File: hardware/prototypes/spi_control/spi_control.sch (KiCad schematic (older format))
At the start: 78 parts, among them J1 USB_B_Micro, J39 Versa_1, J40 Versa_2, U1 ST1L08SPU33R, U2 MCP2210-I_MQ, U3 ADAR7251, U4 BGT24_Module, Y1 12MHZ, Y2 40MHz

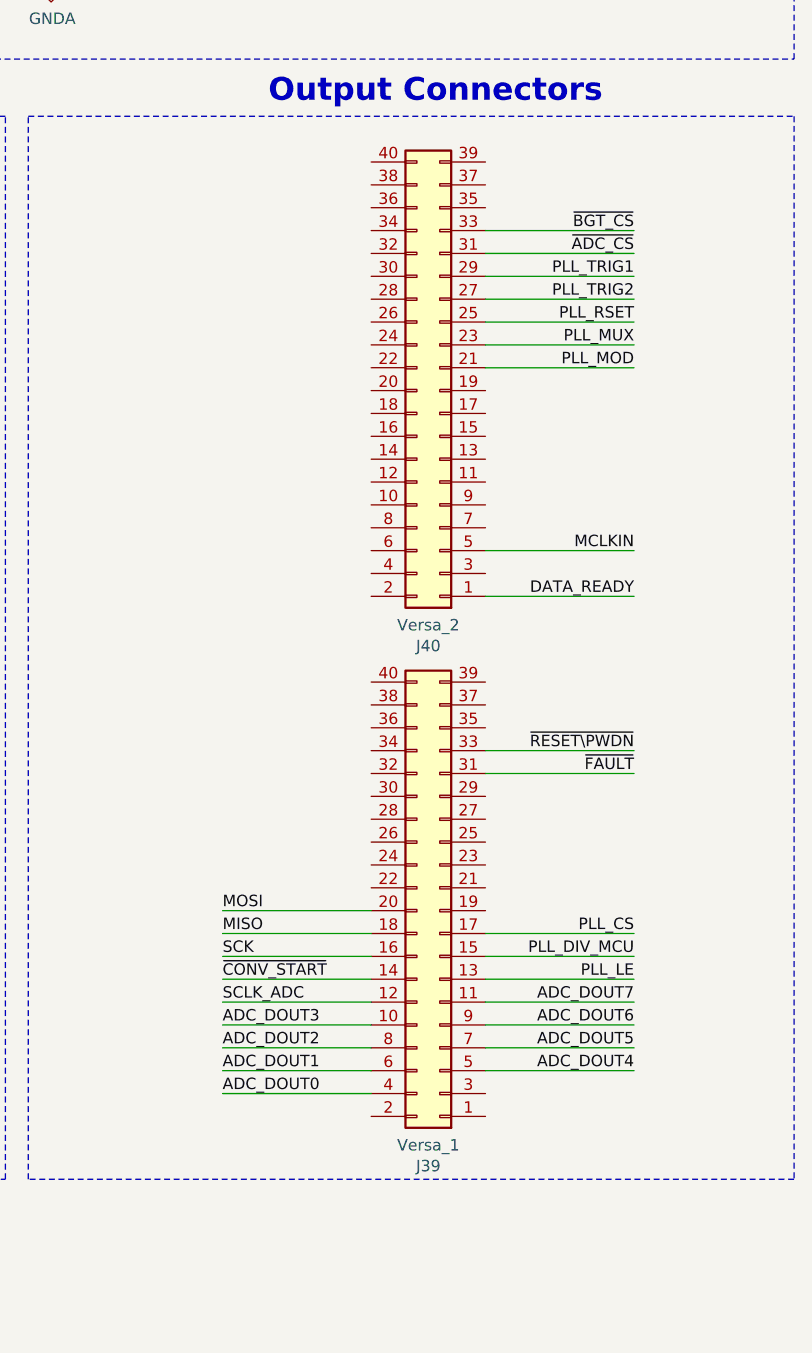
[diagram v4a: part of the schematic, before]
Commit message: Found mistake in header breakout, grounds were not connected. Fixed, layout and schematic.
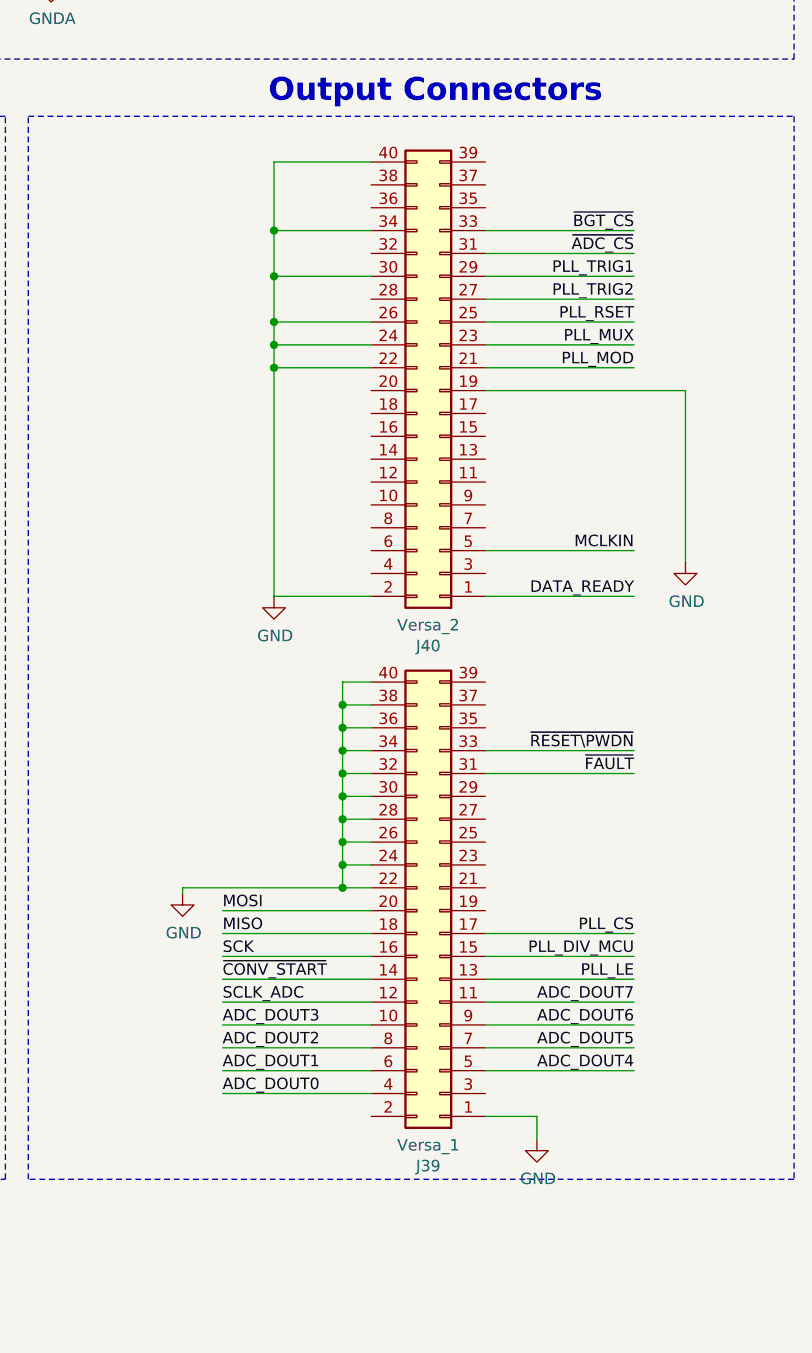
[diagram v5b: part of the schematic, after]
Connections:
- net GND: now also J39.1 (Pin_1), J39.22 (Pin_22), J39.24 (Pin_24), J39.26 (Pin_26), J39.28 (Pin_28), J39.30 (Pin_30), J39.32 (Pin_32), J39.34 (Pin_34), J39.36 (Pin_36), J39.38 (Pin_38), J39.40 (Pin_40), J40.19 (Pin_19), J40.2 (Pin_2), J40.22 (Pin_22), J40.24 (Pin_24), J40.26 (Pin_26), J40.30 (Pin_30), J40.34 (Pin_34), J40.40 (Pin_40)
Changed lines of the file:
@@
 EESchema Schematic File Version 4
 LIBS:spi_control-cache
-EELAYER 30 0
+EELAYER 29 0
 EELAYER END
 $Descr B 17000 11000
@@
 Text Notes 1550 3800 0    100  ~ 20
 RF Transceiver - BGT24 Module
+$Comp
+L power:GND #PWR?
+U 1 1 5DD3FA35
+P 13725 7950
+F 0 "#PWR?" H 13725 7700 50  0001 C CNN
+F 1 "GND" H 13730 7777 50  0000 C CNN
+F 2 "" H 13725 7950 50  0001 C CNN
+F 3 "" H 13725 7950 50  0001 C CNN
+	1    13725 7950
+	1    0    0    -1
+$EndComp
+Wire Wire Line
+	14550 7925 14425 7925
+Wire Wire Line
+	13725 7925 13725 7950
+Wire Wire Line
+	14550 7025 14425 7025
+Wire Wire Line
+	14425 7025 14425 7125
+Connection ~ 14425 7925
+Wire Wire Line
+	14425 7925 13725 7925
+Wire Wire Line
+	14550 7825 14425 7825
+Connection ~ 14425 7825
+Wire Wire Line
+	14425 7825 14425 7925
+Wire Wire Line
+	14550 7725 14425 7725
+Connection ~ 14425 7725
+Wire Wire Line
+	14425 7725 14425 7825
+Wire Wire Line
+	14550 7625 14425 7625
+Connection ~ 14425 7625
+Wire Wire Line
+	14425 7625 14425 7725
+Wire Wire Line
+	14550 7525 14425 7525
+Connection ~ 14425 7525
+Wire Wire Line
+	14425 7525 14425 7625
+Wire Wire Line
+	14550 7425 14425 7425
+Connection ~ 14425 7425
+Wire Wire Line
+	14425 7425 14425 7525
+Wire Wire Line
+	14550 7325 14425 7325
+Connection ~ 14425 7325
+Wire Wire Line
+	14425 7325 14425 7425
+Wire Wire Line
+	14550 7225 14425 7225
+Connection ~ 14425 7225
+Wire Wire Line
+	14425 7225 14425 7325
+Wire Wire Line
+	14550 7125 14425 7125
+Connection ~ 14425 7125
+Wire Wire Line
+	14425 7125 14425 7225
+$Comp
+L power:GND #PWR?
+U 1 1 5DFA6341
+P 15275 9025
+F 0 "#PWR?" H 15275 8775 50  0001 C CNN
+F 1 "GND" H 15280 8852 50  0000 C CNN
+F 2 "" H 15275 9025 50  0001 C CNN
+F 3 "" H 15275 9025 50  0001 C CNN
+	1    15275 9025
+	1    0    0    -1
+$EndComp
+Wire Wire Line
+	15050 8925 15275 8925
+Wire Wire Line
+	15275 8925 15275 9025
+$Comp
+L power:GND #PWR?
+U 1 1 5E0546AE
+P 15925 6500
+F 0 "#PWR?" H 15925 6250 50  0001 C CNN
+F 1 "GND" H 15930 6327 50  0000 C CNN
+F 2 "" H 15925 6500 50  0001 C CNN
+F 3 "" H 15925 6500 50  0001 C CNN
+	1    15925 6500
+	1    0    0    -1
+$EndComp
+Wire Wire Line
+	15050 5750 15925 5750
+Wire Wire Line
+	15925 5750 15925 6500
+Wire Wire Line
+	14550 5650 14125 5650
+Wire Wire Line
+	14550 5550 14125 5550
+Wire Wire Line
+	14550 5450 14125 5450
+Wire Wire Line
+	14125 5450 14125 5550
+Connection ~ 14125 5550
+Wire Wire Line
+	14550 5250 14125 5250
+Wire Wire Line
+	14125 5250 14125 5450
+Connection ~ 14125 5450
+Wire Wire Line
+	14550 5050 14125 5050
+Wire Wire Line
+	14125 5050 14125 5250
+Connection ~ 14125 5250
+Wire Wire Line
+	14550 4750 14125 4750
+Wire Wire Line
+	14125 4750 14125 5050
+Connection ~ 14125 5050
+Wire Wire Line
+	14125 5550 14125 5650
+Connection ~ 14125 5650
+Wire Wire Line
+	14125 5650 14125 6650
+Wire Wire Line
+	14125 6650 14550 6650
+$Comp
+L power:GND #PWR?
+U 1 1 5E40F375
+P 14125 6650
+F 0 "#PWR?" H 14125 6400 50  0001 C CNN
+F 1 "GND" H 14130 6477 50  0000 C CNN
+F 2 "" H 14125 6650 50  0001 C CNN
+F 3 "" H 14125 6650 50  0001 C CNN
+	1    14125 6650
+	1    0    0    -1
+$EndComp
 $EndSCHEMATC

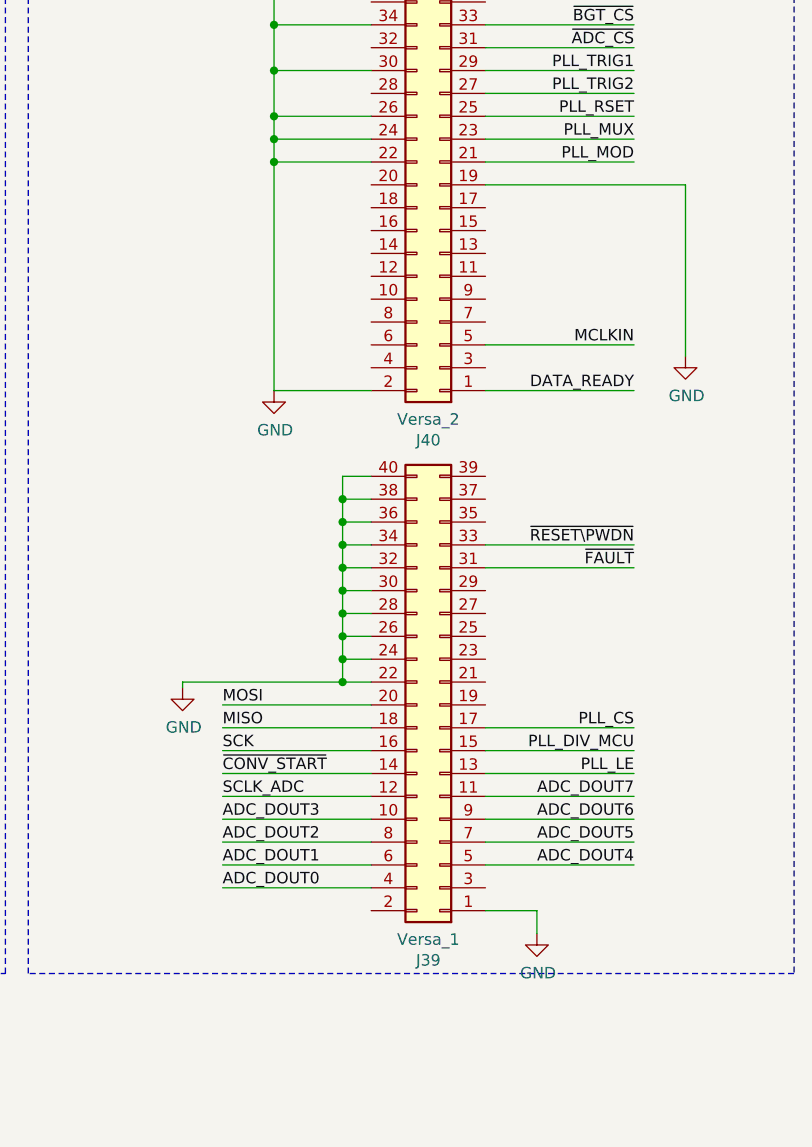
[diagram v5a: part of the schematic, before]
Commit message: Remove Dime scale. Fill on Top layer has no net.  GND Fill on Bottom layer has no net. GND Schematic: Clean up the ground connections on J40, J39, Y2, and Y1. Schematic: Remove ECP5 eval board schematic image. Need to generate BOM. Add NC to J39 and J40 where needed. Change directory “gerbers” to “spi_control_FAB”
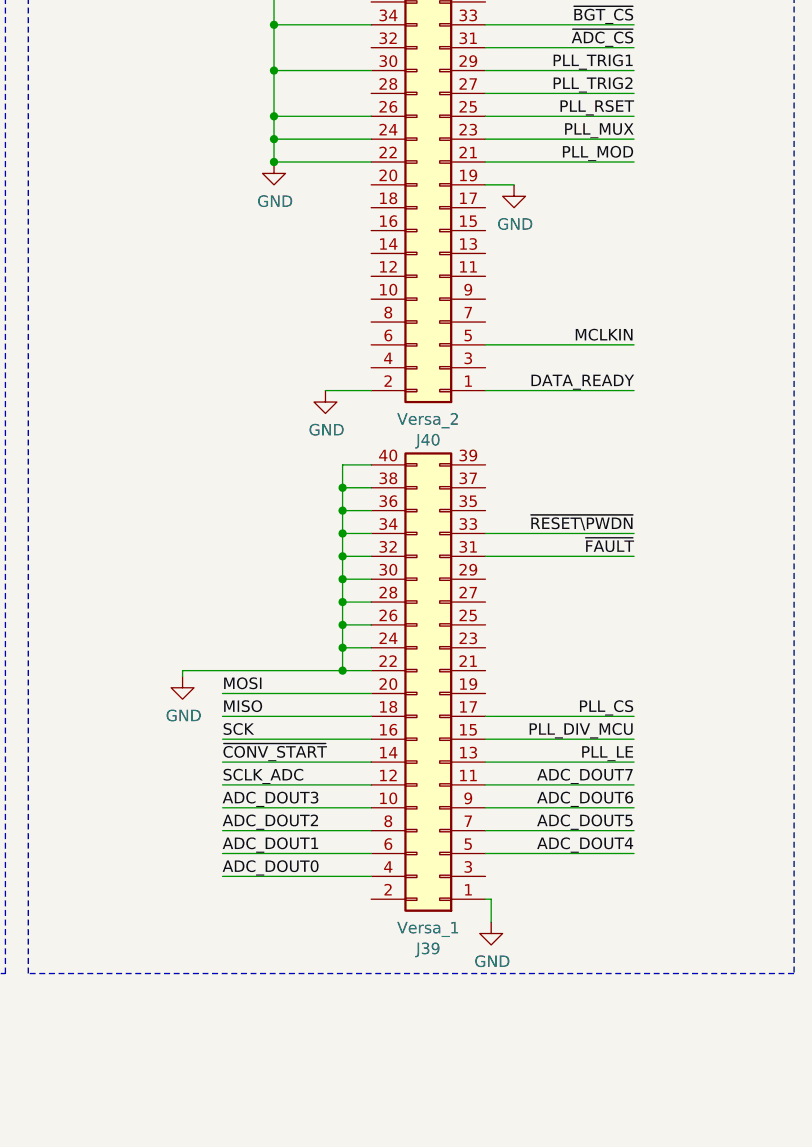
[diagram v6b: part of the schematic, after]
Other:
- moved on the sheet: J39
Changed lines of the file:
@@
 $EndComp
 Wire Wire Line
-	14550 8325 13900 8325
+	14550 8275 13900 8275
 Wire Wire Line
-	15050 7325 15700 7325
+	15050 7275 15700 7275
 Wire Wire Line
-	15050 7425 15700 7425
-Text Label 13900 8325 0    50   ~ 0
+	15050 7375 15700 7375
+Text Label 13900 8275 0    50   ~ 0
 ~CONV_START
 Text Label 15700 6650 2    50   ~ 0
 DATA_READY
-Text Label 15700 7425 2    50   ~ 0
+Text Label 15700 7375 2    50   ~ 0
 ~FAULT
-Text Label 15700 7325 2    50   ~ 0
+Text Label 15700 7275 2    50   ~ 0
 ~RESET\PWDN
 Wire Wire Line
@@
 	15050 5150 15700 5150
 Wire Wire Line
-	14550 8225 13900 8225
+	14550 8175 13900 8175
 Wire Wire Line
-	14550 8025 13900 8025
+	14550 7975 13900 7975
 Wire Wire Line
-	14550 8125 13900 8125
+	14550 8075 13900 8075
 Wire Wire Line
-	15050 8125 15700 8125
+	15050 8075 15700 8075
 Wire Wire Line
 	15050 5050 15700 5050
-Text Label 13900 8125 0    50   ~ 0
+Text Label 13900 8075 0    50   ~ 0
 MISO
-Text Label 13900 8025 0    50   ~ 0
+Text Label 13900 7975 0    50   ~ 0
 MOSI
-Text Label 13900 8225 0    50   ~ 0
+Text Label 13900 8175 0    50   ~ 0
 SCK
-Text Label 15700 8125 2    50   ~ 0
+Text Label 15700 8075 2    50   ~ 0
 PLL_CS
 Text Label 15700 5050 2    50   ~ 0
@@
 L Connector_Generic:Conn_02x20_Odd_Even J39
 U 1 1 5E942031
-P 14850 8025
-F 0 "J39" H 14900 9142 50  0000 C CNN
-F 1 "Versa_1" H 14900 9051 50  0000 C CNN
-F 2 "Connector_PinSocket_2.54mm:PinSocket_2x20_P2.54mm_Vertical_SMD" H 14850 8025 50  0001 C CNN
-F 3 "~" H 14850 8025 50  0001 C CNN
-	1    14850 8025
+P 14850 7975
+F 0 "J39" H 14900 9092 50  0000 C CNN
+F 1 "Versa_1" H 14900 9001 50  0000 C CNN
+F 2 "Connector_PinSocket_2.54mm:PinSocket_2x20_P2.54mm_Vertical_SMD" H 14850 7975 50  0001 C CNN
+F 3 "~" H 14850 7975 50  0001 C CNN
+	1    14850 7975
 	-1   0    0    1
 $EndComp
@@
 Wire Wire Line
 	925  6475 1475 6475
-Text Label 15700 8325 2    50   ~ 0
+Text Label 15700 8275 2    50   ~ 0
 PLL_LE
-Text Label 15700 8225 2    50   ~ 0
+Text Label 15700 8175 2    50   ~ 0
 PLL_DIV_MCU
 Text Label 7450 5250 0    50   ~ 0
@@
 	5150 6000 5850 6000
 Wire Wire Line
-	14550 8525 13900 8525
+	14550 8475 13900 8475
 Wire Wire Line
-	14550 8625 13900 8625
+	14550 8575 13900 8575
 Wire Wire Line
-	14550 8725 13900 8725
+	14550 8675 13900 8675
 Wire Wire Line
-	14550 8825 13900 8825
-Text Label 13900 8425 0    50   ~ 0
+	14550 8775 13900 8775
+Text Label 13900 8375 0    50   ~ 0
 SCLK_ADC
-Text Label 15700 8425 2    50   ~ 0
+Text Label 15700 8375 2    50   ~ 0
 ADC_DOUT7
-Text Label 15700 8525 2    50   ~ 0
+Text Label 15700 8475 2    50   ~ 0
 ADC_DOUT6
-Text Label 15700 8625 2    50   ~ 0
+Text Label 15700 8575 2    50   ~ 0
 ADC_DOUT5
-Text Label 15700 8725 2    50   ~ 0
+Text Label 15700 8675 2    50   ~ 0
 ADC_DOUT4
-Text Label 13900 8525 0    50   ~ 0
+Text Label 13900 8475 0    50   ~ 0
 ADC_DOUT3
-Text Label 13900 8625 0    50   ~ 0
+Text Label 13900 8575 0    50   ~ 0
 ADC_DOUT2
-Text Label 13900 8725 0    50   ~ 0
+Text Label 13900 8675 0    50   ~ 0
 ADC_DOUT1
-Text Label 13900 8825 0    50   ~ 0
+Text Label 13900 8775 0    50   ~ 0
 ADC_DOUT0
 Wire Wire Line
-	14550 8425 13900 8425
+	14550 8375 13900 8375
 Wire Wire Line
-	15050 8425 15700 8425
+	15050 8375 15700 8375
 Wire Wire Line
-	15050 8525 15700 8525
+	15050 8475 15700 8475
 Wire Wire Line
-	15050 8625 15700 8625
+	15050 8575 15700 8575
 Wire Wire Line
-	15050 8725 15700 8725
+	15050 8675 15700 8675
 Wire Wire Line
-	15050 8325 15700 8325
+	15050 8275 15700 8275
 Wire Wire Line
-	15050 8225 15700 8225
+	15050 8175 15700 8175
 $Bitmap
 Pos 18800 3275
@@
 L power:GND #PWR?
 U 1 1 5DD3FA35
-P 13725 7950
-F 0 "#PWR?" H 13725 7700 50  0001 C CNN
-F 1 "GND" H 13730 7777 50  0000 C CNN
-F 2 "" H 13725 7950 50  0001 C CNN
-F 3 "" H 13725 7950 50  0001 C CNN
-	1    13725 7950
+P 13725 7900
+F 0 "#PWR?" H 13725 7650 50  0001 C CNN
+F 1 "GND" H 13730 7727 50  0000 C CNN
+F 2 "" H 13725 7900 50  0001 C CNN
+F 3 "" H 13725 7900 50  0001 C CNN
+	1    13725 7900
 	1    0    0    -1
 $EndComp
 Wire Wire Line
-	14550 7925 14425 7925
+	14550 7875 14425 7875
 Wire Wire Line
-	13725 7925 13725 7950
+	13725 7875 13725 7900
 Wire Wire Line
-	14550 7025 14425 7025
+	14550 6975 14425 6975
 Wire Wire Line
-	14425 7025 14425 7125
-Connection ~ 14425 7925
+	14425 6975 14425 7075
+Connection ~ 14425 7875
 Wire Wire Line
-	14425 7925 13725 7925
+	14425 7875 13725 7875
 Wire Wire Line
-	14550 7825 14425 7825
-Connection ~ 14425 7825
+	14550 7775 14425 7775
+Connection ~ 14425 7775
 Wire Wire Line
-	14425 7825 14425 7925
+	14425 7775 14425 7875
 Wire Wire Line
-	14550 7725 14425 7725
-Connection ~ 14425 7725
+	14550 7675 14425 7675
+Connection ~ 14425 7675
 Wire Wire Line
-	14425 7725 14425 7825
+	14425 7675 14425 7775
 Wire Wire Line
-	14550 7625 14425 7625
-Connection ~ 14425 7625
+	14550 7575 14425 7575
+Connection ~ 14425 7575
 Wire Wire Line
-	14425 7625 14425 7725
+	14425 7575 14425 7675
 Wire Wire Line
-	14550 7525 14425 7525
-Connection ~ 14425 7525
+	14550 7475 14425 7475
+Connection ~ 14425 7475
 Wire Wire Line
-	14425 7525 14425 7625
+	14425 7475 14425 7575
 Wire Wire Line
-	14550 7425 14425 7425
-Connection ~ 14425 7425
+	14550 7375 14425 7375
+Connection ~ 14425 7375
 Wire Wire Line
-	14425 7425 14425 7525
+	14425 7375 14425 7475
 Wire Wire Line
-	14550 7325 14425 7325
-Connection ~ 14425 7325
+	14550 7275 14425 7275
+Connection ~ 14425 7275
 Wire Wire Line
-	14425 7325 14425 7425
+	14425 7275 14425 7375
 Wire Wire Line
-	14550 7225 14425 7225
-Connection ~ 14425 7225
+	14550 7175 14425 7175
+Connection ~ 14425 7175
 Wire Wire Line
-	14425 7225 14425 7325
+	14425 7175 14425 7275
 Wire Wire Line
-	14550 7125 14425 7125
-Connection ~ 14425 7125
+	14550 7075 14425 7075
+Connection ~ 14425 7075
 Wire Wire Line
-	14425 7125 14425 7225
+	14425 7075 14425 7175
 $Comp
 L power:GND #PWR?
 U 1 1 5DFA6341
-P 15275 9025
-F 0 "#PWR?" H 15275 8775 50  0001 C CNN
-F 1 "GND" H 15280 8852 50  0000 C CNN
-F 2 "" H 15275 9025 50  0001 C CNN
-F 3 "" H 15275 9025 50  0001 C CNN
-	1    15275 9025
+P 15075 8975
+F 0 "#PWR?" H 15075 8725 50  0001 C CNN
+F 1 "GND" H 15080 8802 50  0000 C CNN
+F 2 "" H 15075 8975 50  0001 C CNN
+F 3 "" H 15075 8975 50  0001 C CNN
+	1    15075 8975
 	1    0    0    -1
 $EndComp
 Wire Wire Line
-	15050 8925 15275 8925
-Wire Wire Line
-	15275 8925 15275 9025
+	15075 8875 15075 8975
 $Comp
 L power:GND #PWR?
 U 1 1 5E0546AE
-P 15925 6500
-F 0 "#PWR?" H 15925 6250 50  0001 C CNN
-F 1 "GND" H 15930 6327 50  0000 C CNN
-F 2 "" H 15925 6500 50  0001 C CNN
-F 3 "" H 15925 6500 50  0001 C CNN
-	1    15925 6500
+P 15175 5750
+F 0 "#PWR?" H 15175 5500 50  0001 C CNN
+F 1 "GND" H 15180 5577 50  0000 C CNN
+F 2 "" H 15175 5750 50  0001 C CNN
+F 3 "" H 15175 5750 50  0001 C CNN
+	1    15175 5750
 	1    0    0    -1
 $EndComp
 Wire Wire Line
-	15050 5750 15925 5750
-Wire Wire Line
-	15925 5750 15925 6500
+	15050 5750 15175 5750
 Wire Wire Line
 	14550 5650 14125 5650
@@
 Wire Wire Line
 	14125 5550 14125 5650
-Connection ~ 14125 5650
-Wire Wire Line
-	14125 5650 14125 6650
-Wire Wire Line
-	14125 6650 14550 6650
 $Comp
 L power:GND #PWR?
 U 1 1 5E40F375
-P 14125 6650
-F 0 "#PWR?" H 14125 6400 50  0001 C CNN
-F 1 "GND" H 14130 6477 50  0000 C CNN
-F 2 "" H 14125 6650 50  0001 C CNN
-F 3 "" H 14125 6650 50  0001 C CNN
-	1    14125 6650
+P 14125 5650
+F 0 "#PWR?" H 14125 5400 50  0001 C CNN
+F 1 "GND" H 14130 5477 50  0000 C CNN
+F 2 "" H 14125 5650 50  0001 C CNN
+F 3 "" H 14125 5650 50  0001 C CNN
+	1    14125 5650
+	1    0    0    -1
+$EndComp
+Connection ~ 14125 5650
+$Comp
+L power:GND #PWR?
+U 1 1 5DE12E51
+P 14350 6650
+F 0 "#PWR?" H 14350 6400 50  0001 C CNN
+F 1 "GND" H 14355 6477 50  0000 C CNN
+F 2 "" H 14350 6650 50  0001 C CNN
+F 3 "" H 14350 6650 50  0001 C CNN
+	1    14350 6650
 	1    0    0    -1
 $EndComp
+Wire Wire Line
+	14350 6650 14550 6650
+Wire Wire Line
+	15050 8875 15075 8875
 $EndSCHEMATC

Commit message: Nov 17 Issues 1-22 complete.
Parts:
- added H1, H2, H3, H4, H5, H6: MountingHole, MountingHole_2.2mm_M2_Pad_Via, symbol Mechanical:MountingHole_Pad
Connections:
- net GND: now also H1.1, H2.1, H3.1, H4.1, H5.1, H6.1
- no-connect marks 2 -> 35
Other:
- moved on the sheet: C25, C26, R5, R6, R7, Y2
